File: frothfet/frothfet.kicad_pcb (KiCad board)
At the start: 4 copper layers, 144 x 127 mm, 356 parts, among them J1 Screw_Terminal_01x08, J2 Screw_Terminal_01x08, J3 USB_TYPE_C_16PIN, M1 Fan_Tacho, M2 Fan_Tacho, Q1 AO3400A, Q10 BSC010N04LS, Q11 AO3400A, Q12 BSC010N04LS, Q13 AO3400A, Q14 BSC010N04LS, Q15 AO3400A, Q16 BSC010N04LS, Q17 AO3400A, Q18 AO3400A, Q19 AO3400A, Q2 BSC010N04LS, Q20 FDC6330L, Q21 S8050, Q22 S8050, Q3 AO3400A, Q4 BSC010N04LS, Q5 AO3400A, Q6 BSC010N04LS, Q7 AO3400A, Q8 BSC010N04LS, Q9 AO3400A, SW1 RESET, SW2 BOOT, U1 SN74LVC1G14DBV, U10 SN74LVC1G14DBV, U11 LM74502H, U12 TMCS1108A2U, U13 SN74LVC1G14DBV, U14 LM74502H, U15 TMCS1108A2U, U16 SN74LVC1G14DBV, U17 LM74502H, U18 TMCS1108A2U, U19 SN74LVC1G14DBV, U2 LM74502H, U20 LM74502H, U21 TMCS1108A2U, U22 SN74LVC1G14DBV, U23 LM74502H, U24 TMCS1108A2U, U25 MCP3564R, U26 MCP3564R, U27 TPS7A2033PDBVR, U28 MCP3425A0T-ECH, U29 REF35330QDBVR, U3 TMCS1108A2U, U30 XL1509-5.0, U31 ESP32-S3-WROOM-1-N16R8, U32 USBLC6-2SC6, U33 XC6210B332MR, U34 CH334F, U35 CH343P, U4 SN74LVC1G14DBV, U5 LM74502H, U6 TMCS1108A2U, U7 SN74LVC1G14DBV, U8 LM74502H, U9 TMCS1108A2U, Y1 12Mhz, Y2 32.768kHz

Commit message: bom and placement all check out.  ready for production!
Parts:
- D36, D43: value LED -> RED
- R89: value 1k -> 10k
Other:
- board text removed: "YARRBOARD"

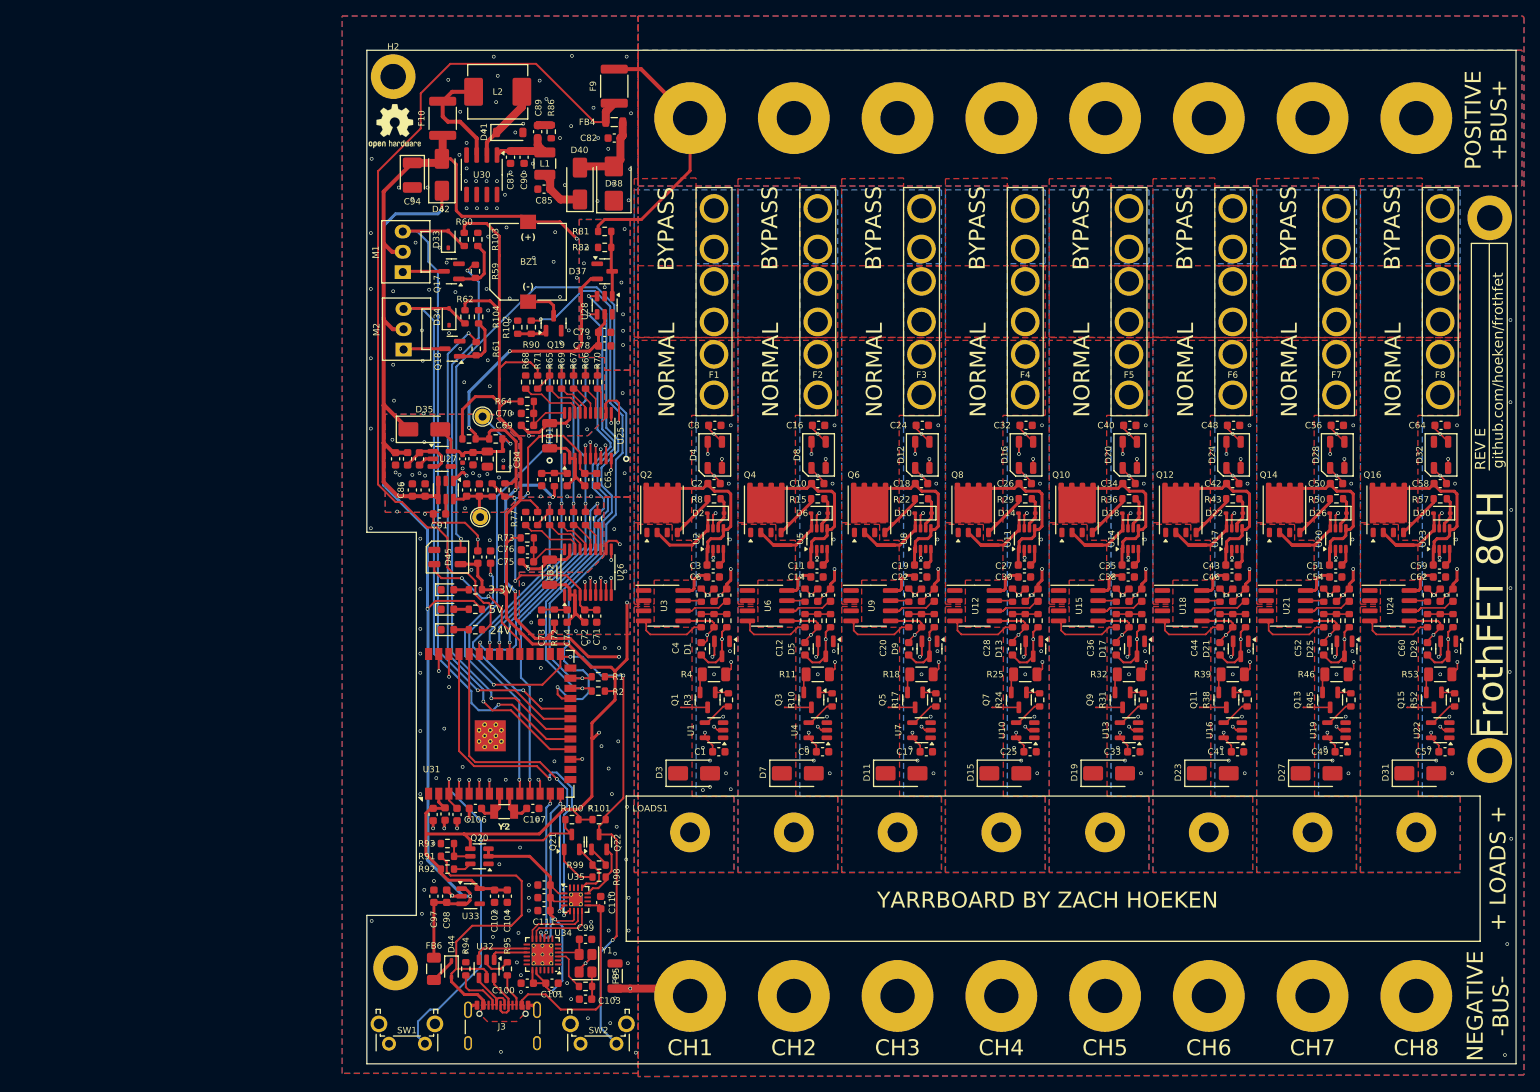
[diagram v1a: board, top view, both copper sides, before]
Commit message: rounded board edges
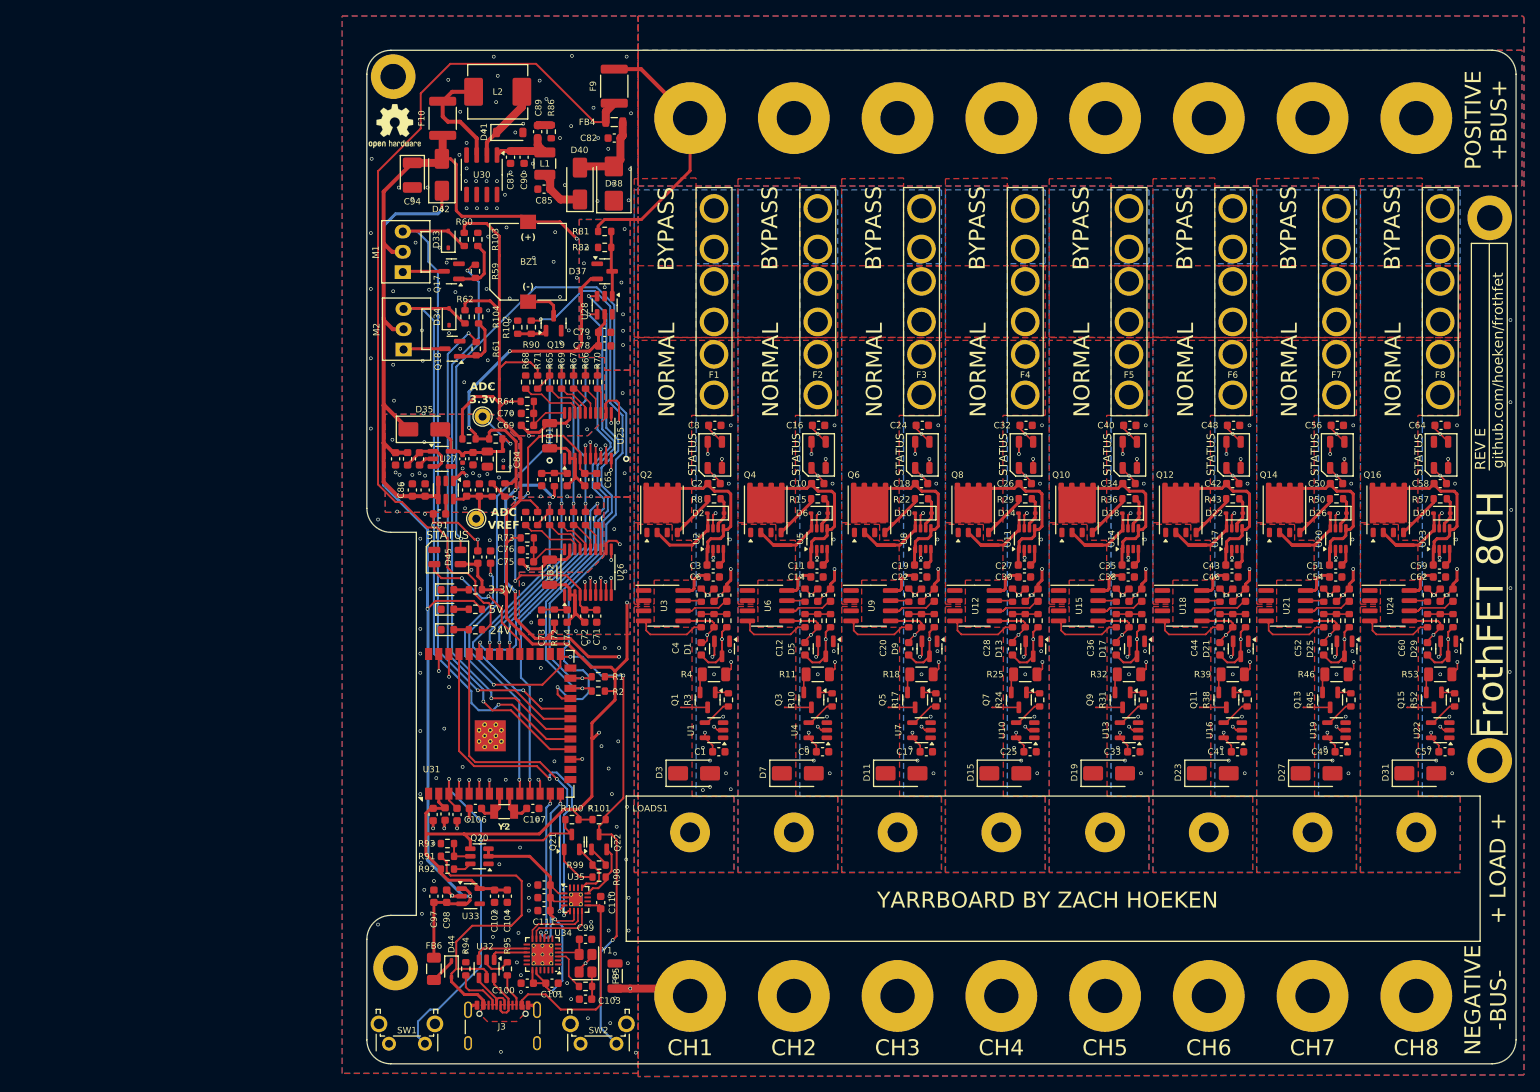
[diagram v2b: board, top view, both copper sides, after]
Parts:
- moved TP2 0.54 mm to (66.7, 86.7)
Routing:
- net GND: track 212.5 -> 212.2 mm, vias 327 -> 324
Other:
- outline, holes or cut-outs redrawn
- board text added: "+ LOAD +"
- board text added: "ADC 3.3v"
- board text added: "ADC VREF"
- board text added: "STATUS"
- board text removed: "+ LOADS +"

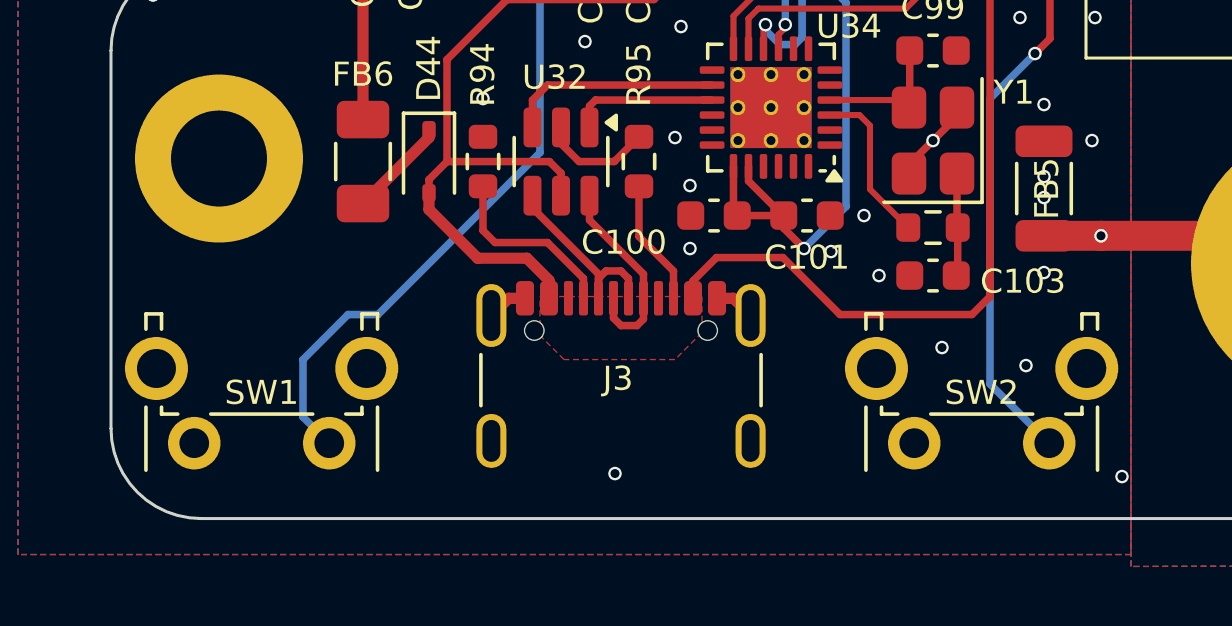
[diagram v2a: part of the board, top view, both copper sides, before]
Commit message: updated busbar design and added button silkscreen
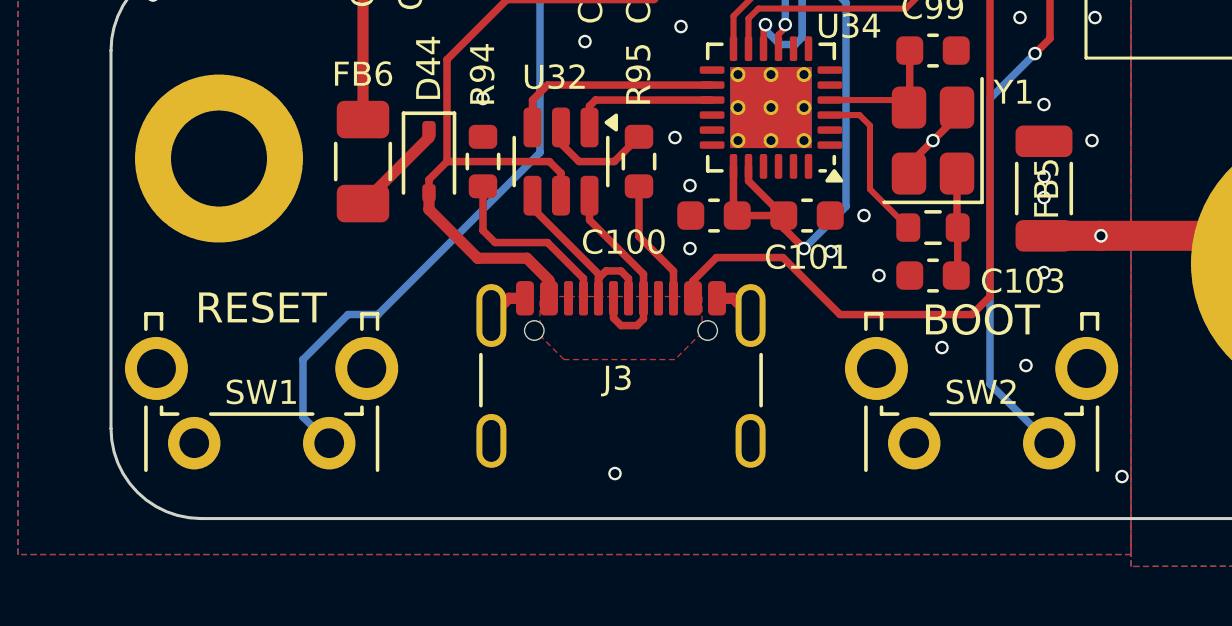
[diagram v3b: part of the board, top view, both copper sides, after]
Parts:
- J1: footprint yarrboard:Busbar Rev E -> yarrboard:Frothfet Busbar Positive Rev E
- J2: footprint yarrboard:Busbar Rev E -> yarrboard:Frothfet Busbar Negative Rev E
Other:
- board text added: "BOOT"
- board text added: "RESET"
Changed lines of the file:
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@@
 		)
 	)
-	(footprint "yarrboard:Busbar Rev E"
+	(footprint "yarrboard:Frothfet Busbar Positive Rev E"
 		(layer "B.Cu")
 		(at 93.5 36.5)
@@
 			(effects
 				(font
-					(size 0.8 0.8)
+					(size 1 1)
 					(thickness 0.1)
 				)
@@
 		(sheetname "/Power Supply/")
 		(sheetfile "power.kicad_sch")
-		(attr through_hole exclude_from_bom)
+		(attr through_hole exclude_from_pos_files exclude_from_bom)
 		(fp_line
 			(start -6 3.5)
@@
 		(fp_line
 			(start -1.000001 8.5)
-			(end 124 8.5)
+			(end 149 8.5)
 			(stroke
 				(width 0.2)
@@
 		)
 		(fp_line
-			(start 124 -8.5)
+			(start 149 -8.5)
 			(end -1 -8.5)
 			(stroke
@@
 		)
 		(fp_line
-			(start 129 3.5)
-			(end 129 -3.5)
+			(start 154 3.5)
+			(end 154 -3.5)
 			(stroke
 				(width 0.2)
@@
 		)
 		(fp_arc
-			(start 124 -8.5)
-			(mid 127.535534 -7.035534)
-			(end 129 -3.5)
+			(start 149 -8.5)
+			(mid 152.535534 -7.035534)
+			(end 154 -3.5)
 			(stroke
 				(width 0.2)
@@
 		)
 		(fp_arc
-			(start 129 3.5)
-			(mid 127.535534 7.035534)
-			(end 124 8.5)
+			(start 154 3.5)
+			(mid 152.535534 7.035534)
+			(end 149 8.5)
 			(stroke
 				(width 0.2)
@@
 		)
 		(fp_circle
-			(center 117 0)
-			(end 120.4 0)
+			(center 142 0)
+			(end 145.4 0)
 			(stroke
 				(width 0.2)
@@
 		)
 		(group ""
-			(members "011ee016-82c5-4748-99cf-804eb24ccc96" "11dfe296-c508-4c2c-b41f-c7efb9fb8ab4"
-				"17fb8aea-a37a-487a-8fc5-2aa3b4636a5d" "19528700-45c3-4459-894c-06c804ed3e6a"
-				"36bc9cf0-08cd-4623-a119-07dd1c9881c4" "40a22c53-9b08-4635-a18b-adf08647706d"
-				"8733a5a5-c571-455b-803f-b5c79c1f3b27" "889f2a5e-a654-4ca0-8652-36e17062e277"
-				"8f6ef9d2-5d46-4e8e-8213-51b0b022967f" "9c43f1bd-855e-4ab6-9e0d-9fe28a6fed45"
-				"cb226617-6814-44a9-bc90-f0b98f0a7714" "d31f6164-613f-4f0e-a7e8-9e807375ef56"
-				"d3a307ae-b473-4e50-a045-53eaa0507302" "d5db6869-e428-4347-a942-60a3cc2c6cfe"
-				"edc8ac9d-f480-4727-98b0-ae07031677f0" "f05ba0a6-c5f8-47c8-9bed-42821222e731"
-				"f58ecee1-a206-4837-b1ff-646567d0c1b2"
+			(members "06d6ce2e-d91f-4845-94d5-1ad209b3ac7b" "0784c3f0-90e7-4858-9cd7-ac6a698e9736"
+				"083888fe-6747-493a-b666-849f20d3d326" "1190d6be-011f-4a24-ba54-8e28285dd198"
+				"15009c6e-5599-49d6-8871-46eb71dba2f8" "17ce69dd-fa85-4f5c-a169-8a2b3652214a"
+				"1bdf373e-8612-433b-a96f-9d345424d47f" "24629c94-5bcc-44d3-9d51-b1dabcb0336f"
+				"450cd0a6-a926-44ea-9951-fe8fc65e12e0" "48107d2f-d77a-4bb7-94a9-d584571b663a"
+				"54e74a54-1c6c-4b7f-8fce-1efe123fd146" "668ea8d9-dd18-47b7-86c5-ae13576d111b"
+				"7327bae7-7bca-4c21-8560-1914736231d4" "85fc8120-e93d-467f-ba73-2db86d60a0c9"
+				"99f89944-8027-477a-92c3-357adb3940ca" "cfa2b2c5-4b9f-4dd9-8846-1747f1a4deb8"
+				"d5c3b2b7-07b8-408d-bb90-b8443d9c11e4"
 			)
 		)
 		(embedded_fonts no)
-		(model "/Users/hoeken/github/yarrboard-hardware/models/busbar-rev-e.step"
+		(model "/Users/hoeken/github/yarrboard-hardware/models/busbar-positive-rev-e.step"
 			(offset
 				(xyz 0 0 0)
@@
 		)
 	)
-	(footprint "yarrboard:Busbar Rev E"
+	(footprint "yarrboard:Frothfet Busbar Negative Rev E"
 		(layer "B.Cu")
 		(at 93.5 146.5)
@@
 			(effects
 				(font
-					(size 0.8 0.8)
+					(size 1 1)
 					(thickness 0.1)
 				)
@@
 		(sheetname "/Power Supply/")
 		(sheetfile "power.kicad_sch")
-		(attr through_hole exclude_from_bom)
+		(attr through_hole exclude_from_pos_files exclude_from_bom)
 		(fp_line
 			(start -6 3.5)
@@
 		)
 		(group ""
-			(members "06f42f96-c287-40ea-82c2-1ff583b5afda" "10892e7c-1100-4cbb-a840-310c443ba168"
-				"13087e65-614c-4692-b9d3-6879c08d51d9" "16f9570f-a509-40c3-8da0-3bab5688fc9a"
-				"38d0804c-37c9-4380-ad6a-40a9898ac633" "47756e7b-6f09-4604-80a3-91b3a723932b"
-				"526558c6-7684-41ae-8f4d-bd90ea64a60c" "577499b0-96bc-4c14-aac4-b28faad179d7"
-				"64f8ab1c-c3a0-4c40-b11e-28209ebd2ac9" "68850efd-3cb3-4b16-9275-989434924443"
-				"695a531e-8e51-405e-95af-ea2a78e1e602" "6aec5e34-baf9-4aff-ab62-24e472179566"
-				"7f12008b-fdab-43c6-9d6c-297047302d48" "8138f110-9bdc-4c75-9c78-9871ecd1aa7d"
-				"b1fe3069-c5b6-4a60-8dfd-01590d3c1909" "cda71638-7c2b-4e36-b57f-223ea01900c4"
-				"fc38b93b-87b9-4c4a-bb1d-3cedaa20f358"
+			(members "0f2b3ca8-b5f5-42a6-93ac-db01e0adc6a3" "10b471dd-3d9a-4d63-99c5-3bfdc2d5bbd3"
+				"1928ddd9-f222-4a9d-bfb8-384050f450d8" "23162f7b-09f8-4b05-a68d-e0ee7564504e"
+				"3a534730-173f-48d7-9892-cf93fe8db8a0" "86c39580-4538-43df-8e6b-de43638a51ea"
+				"8b5a01bd-ae72-410b-8571-2990ddfa566b" "8d94dcac-d29c-4d55-a38b-093d8f0c39d7"
+				"9414c8d6-2801-4357-8442-de18d53662ff" "b3cc1822-7ab1-4887-ae1c-5665d8635025"
+				"b4406e3a-eb2d-4ee9-9cb5-39dbdd9d5c06" "bc4c7e0b-e920-419b-a16e-698cbb6d3bde"
+				"c3fbbde3-6908-4aef-9a45-0a9f20144feb" "e1794118-7a58-4676-9de3-9d5deda4bd63"
+				"efe67f48-b71e-4ba3-9ae6-29a8448c609e" "f73ad380-561d-4d26-bafa-a03d95e18d43"
+				"fb2f6d73-add3-4a60-9c25-9d660ef8f6a0"
 			)
 		)
 		(embedded_fonts no)
-		(model "/Users/hoeken/github/yarrboard-hardware/models/busbar-rev-e.step"
+		(model "/Users/hoeken/github/yarrboard-hardware/models/busbar-negative-rev-e.step"
 			(offset
 				(xyz 0 0 0)
@@
 		)
 	)
+	(gr_text "BOOT"
+		(at 82 148.4 0)
+		(layer "F.SilkS" knockout)
+		(effects
+			(font
+				(size 1 1)
+				(thickness 0.15)
+			)
+		)
+	)
 	(gr_text "NEGATIVE\n-BUS-"
 		(locked yes)
@@
 		(layer "F.SilkS" knockout)
 		(effects
+			(font
+				(size 1 1)
+				(thickness 0.15)
+			)
+		)
+	)
+	(gr_text "RESET"
+		(at 58 148 0)
+		(layer "F.SilkS" knockout)
+		(effects
